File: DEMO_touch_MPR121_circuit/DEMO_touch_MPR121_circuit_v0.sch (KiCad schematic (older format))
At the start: 16 parts, among them Q1 IPP060N06N, Q2 IPP060N06N, Q3 IPP060N06N, U1 ARDUINO_R3_ICSP, U2 MPR121_Arduino_shield, U4 VREG_board_MAKERFACTORY

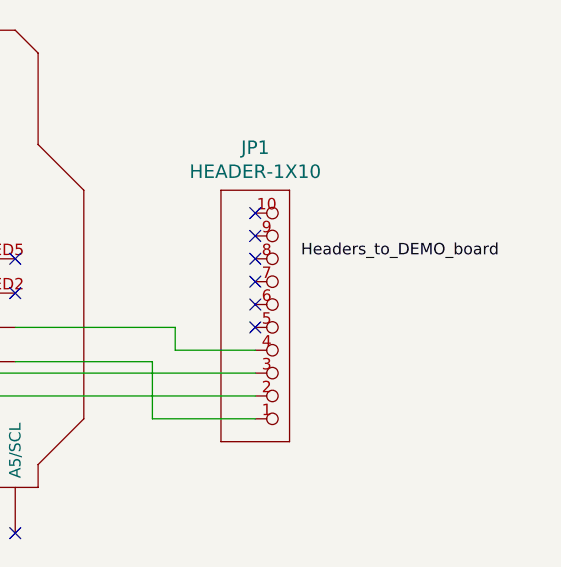
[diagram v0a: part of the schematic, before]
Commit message: Circuit schematics update + LED power test sketch added
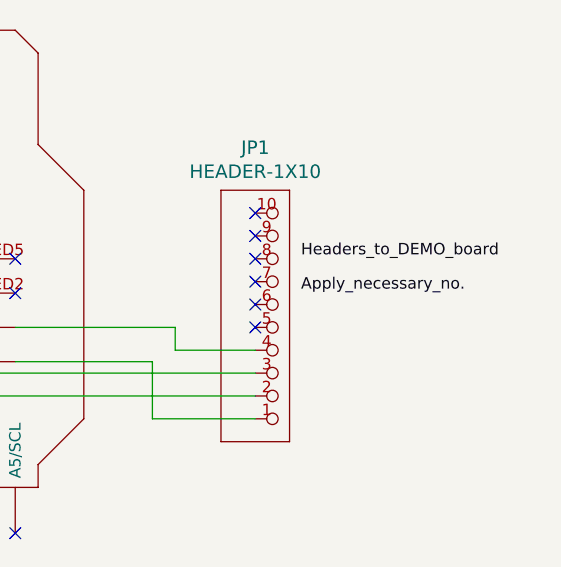
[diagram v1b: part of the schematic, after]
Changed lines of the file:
@@
 Connection ~ 1450 1700
 Connection ~ 1450 2200
+Text Label 10100 4900 0    50   ~ 0
+Apply_necessary_no.
 $EndSCHEMATC
